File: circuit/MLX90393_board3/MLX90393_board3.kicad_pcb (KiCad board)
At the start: 4 copper layers, 60.4 x 43.4 mm, 28 parts, among them J1 Conn_02x04_Odd_Even, Q1 BSS138, Q2 BSS138, U5 AP2112K-3.3

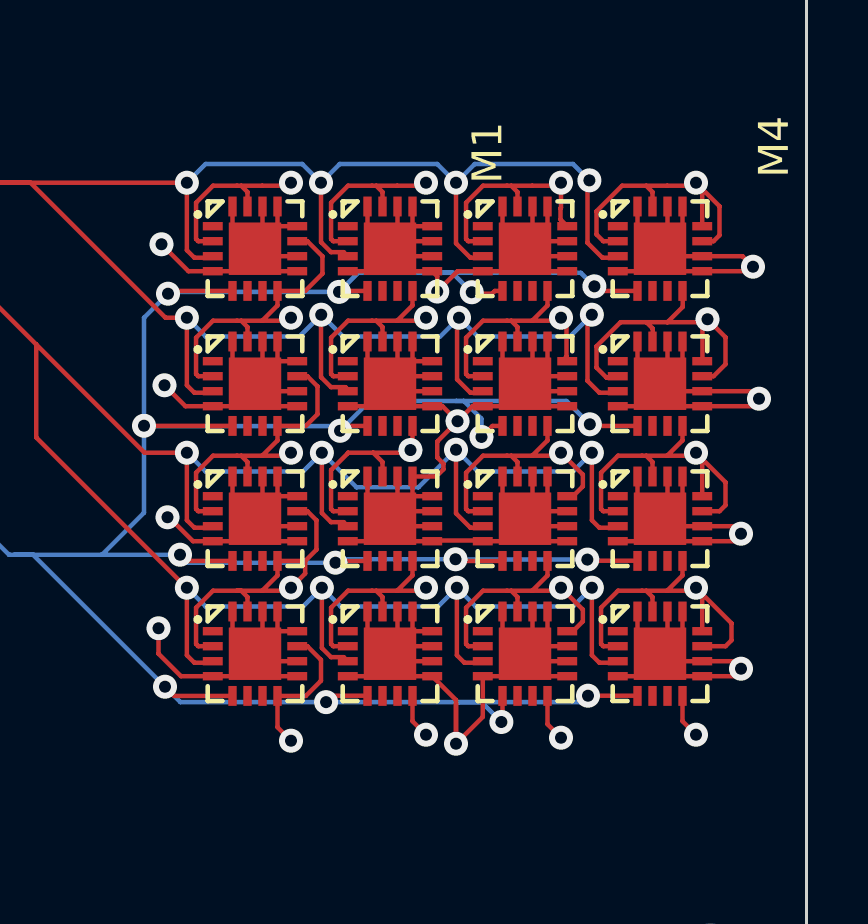
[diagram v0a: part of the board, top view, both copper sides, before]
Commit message: refactored socketio
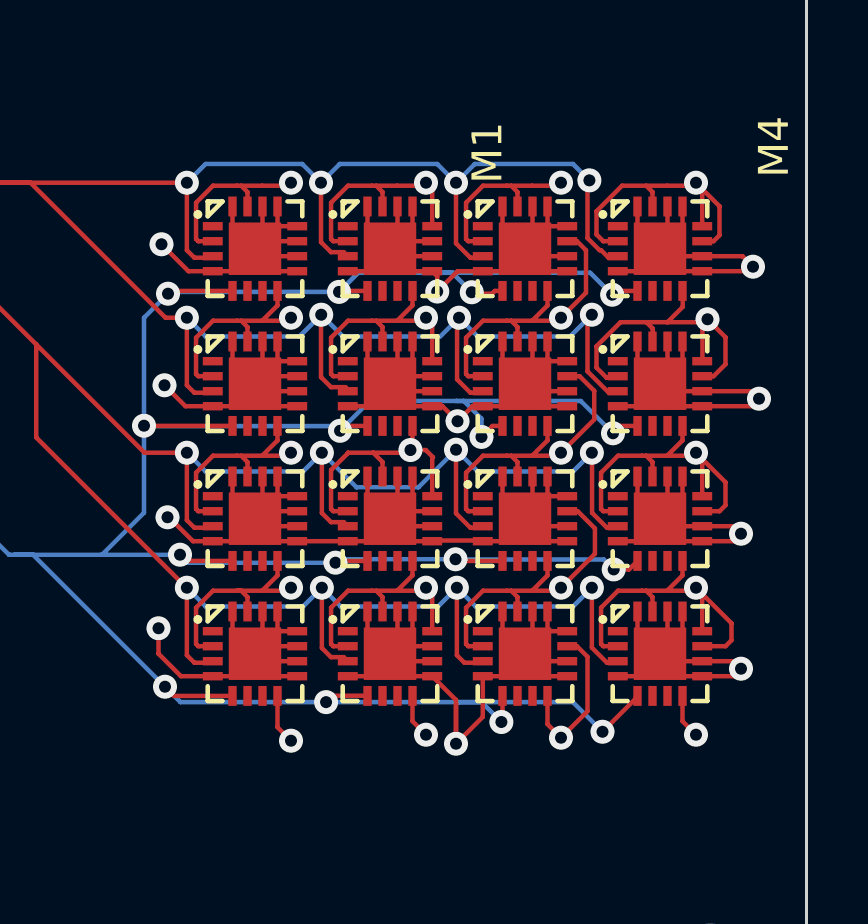
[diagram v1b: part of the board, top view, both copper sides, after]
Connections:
- D1 pad 1: +3.3V -> GND
- D1 pad 2: GND -> +3.3V
- M1 pad 12: GND -> +3.3V
- M10 pad 12: GND -> +3.3V
- M11 pad 11: GND -> +3.3V
- M11 pad 12: +3.3V -> GND
- M13 pad 11: +3.3V -> GND
- M14 pad 12: GND -> +3.3V
- M15 pad 11: GND -> +3.3V
- M15 pad 12: +3.3V -> GND
- M2 pad 11: GND -> +3.3V
- M2 pad 12: +3.3V -> GND
- M3 pad 11: +3.3V -> GND
- M5 pad 11: +3.3V -> GND
- M6 pad 12: GND -> +3.3V
- M7 pad 11: GND -> +3.3V
- M7 pad 12: +3.3V -> GND
- M9 pad 11: +3.3V -> GND
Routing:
- net SDA_3V: track 123.8 -> 125.4 mm
- net +3.3V: track 192.2 -> 191.6 mm
- net SCL_3V: track 160.7 -> 160.1 mm
